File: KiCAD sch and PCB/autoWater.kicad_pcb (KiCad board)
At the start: 2 copper layers, 20.1 x 74.9 mm, 0 parts

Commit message: some commit
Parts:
- added C1: 0.1uF, Capacitor_SMD:C_0805_2012Metric_Pad1.15x1.40mm_HandSolder, F.Cu at (46.0, 79.0)
- added D1: LED, LED_SMD:LED_0805_2012Metric_Pad1.15x1.40mm_HandSolder, F.Cu at (53.0, 46.0)
- added J1: Li-ion 18650, Connector_PinHeader_2.54mm:PinHeader_1x02_P2.54mm_Vertical, F.Cu at (49.8, 79.0)
- added J2: PROG, Connector_PinHeader_2.54mm:PinHeader_1x05_P2.54mm_Vertical, F.Cu at (42.2, 67.8)
- added J3: Water Pump, Connector_PinHeader_2.54mm:PinHeader_1x02_P2.54mm_Vertical, F.Cu at (49.0, 62.0)
- added J4: Soil Humidity Sensor, Connector_PinHeader_2.54mm:PinHeader_1x02_P2.54mm_Vertical, F.Cu at (41.0, 60.0)
- added Q1: AO3400, Package_TO_SOT_SMD:SOT-23, F.Cu at (40.6, 53.3)
- added Q2: AO3400, Package_TO_SOT_SMD:SOT-23, F.Cu at (29.2, 54.1)
- added R1: 470, Resistor_SMD:R_0805_2012Metric_Pad1.15x1.40mm_HandSolder, F.Cu at (57.0, 62.0)
- added R2: 4.7k, Resistor_THT:R_Axial_DIN0411_L9.9mm_D3.6mm_P15.24mm_Horizontal, F.Cu at (30.2, 82.0)
- added R3: 1.5k, Resistor_THT:R_Axial_DIN0411_L9.9mm_D3.6mm_P15.24mm_Horizontal, F.Cu at (59.7, 73.2)
- added R4: 10k, Resistor_SMD:R_0805_2012Metric_Pad1.15x1.40mm_HandSolder, F.Cu at (39.4, 71.9)
- added R5: 10k, Resistor_SMD:R_0805_2012Metric_Pad1.15x1.40mm_HandSolder, F.Cu at (54.7, 77.3)
- added R6: 470k, Resistor_SMD:R_0805_2012Metric_Pad1.15x1.40mm_HandSolder, F.Cu at (49.0, 46.0)
- added R7: 150k, Resistor_SMD:R_0805_2012Metric_Pad1.15x1.40mm_HandSolder, F.Cu at (47.5, 67.3)
- added SW1: SW_Push_Dual, Button_Switch_SMD:SW_SPST_Omron_B3FS-100xP, F.Cu at (63.8, 86.2)
- added U1: ATtiny13-20SSU, Package_SO:SOIC-8_3.9x4.9mm_P1.27mm, F.Cu at (48.6, 73.5)
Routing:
- net Net-(J2-Pad1): track 0.00 -> 13.9 mm
- net Net-(J2-Pad3): track 0.00 -> 6.73 mm
- net +5V: track 0.00 -> 6.48 mm
- net Net-(J2-Pad2): track 0.00 -> 4.47 mm

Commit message: new pcb
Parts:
- C1, D1, J1, J2, J3, J4, Q1, Q2, R1, R2, R3, R4, R5, R6, R7, SW1, U1: moved to B.Cu
- moved D1 47.2 mm to (42.3, 91.9), turned to 180 degrees
- moved R6 44.2 mm to (42.3, 89.7), turned to 180 degrees
- moved Q1 36.8 mm to (46.1, 89.7), turned to 180 degrees
- moved J4 36.5 mm to (47.0, 96.0), turned to 0 degrees
- moved Q2 26.5 mm to (49.5, 71.3)
- moved R2 25.7 mm to (51.8, 96.0)
- moved R1 25.1 mm to (40.1, 80.5)
- moved SW1 24.3 mm to (54.0, 63.9)
- moved J2 14.2 mm to (42.9, 82.0)
- moved R7 13.8 mm to (46.0, 81.0), turned to 270 degrees
- moved J1 13.8 mm to (46.7, 65.5), turned to 90 degrees
- moved C1 7.88 mm to (45.7, 71.1), turned to 90 degrees
- moved R3 5.21 mm to (56.1, 77.0), turned to 270 degrees
- moved R4 4.13 mm to (40.1, 75.9)
- moved R5 3.88 mm to (55.1, 73.4), turned to 0 degrees
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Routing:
- net +5V: track 6.48 -> 44.9 mm
- net Net-(J2-Pad3): track 6.73 -> 25.4 mm, vias 0 -> 2
- net Net-(J3-Pad2): track 0.00 -> 15.3 mm
- net GND: track 0.00 -> 13.2 mm, vias 0 -> 4
- net Button: track 0.00 -> 11.3 mm
- net Net-(R2-Pad2): track 0.00 -> 11.0 mm
- net Net-(D1-Pad2): track 0.00 -> 10.9 mm
- net Net-(Q2-Pad1): track 0.00 -> 8.95 mm
- net Net-(J2-Pad1): track 13.9 -> 19.0 mm
- net Sensor: track 0.00 -> 4.83 mm
- net Sensor_Voltage: track 0.00 -> 2.85 mm
- net Net-(J2-Pad2): track 4.47 -> 6.50 mm
- added copper zone on B.Cu, net GND
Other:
- board size 20.1 x 74.9 mm -> 20.8 x 41.4 mm

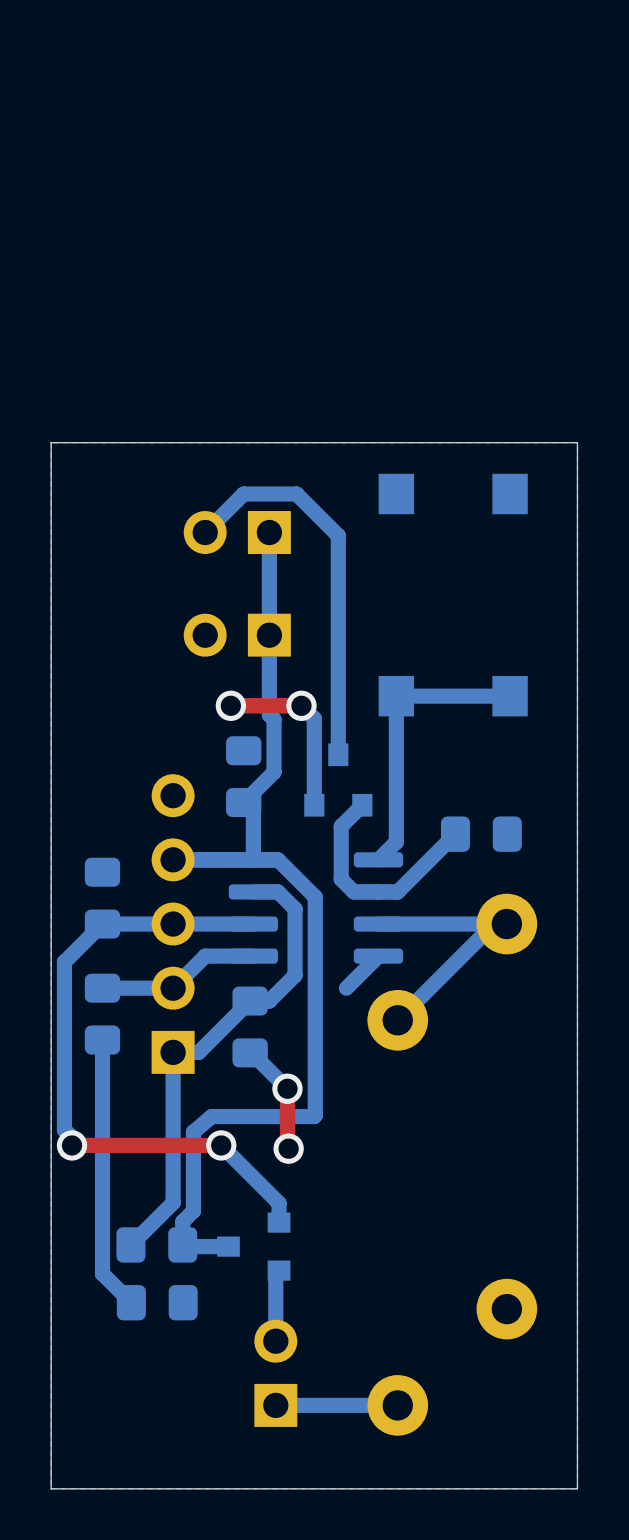
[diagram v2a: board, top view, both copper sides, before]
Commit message: added li ion charger on pcb
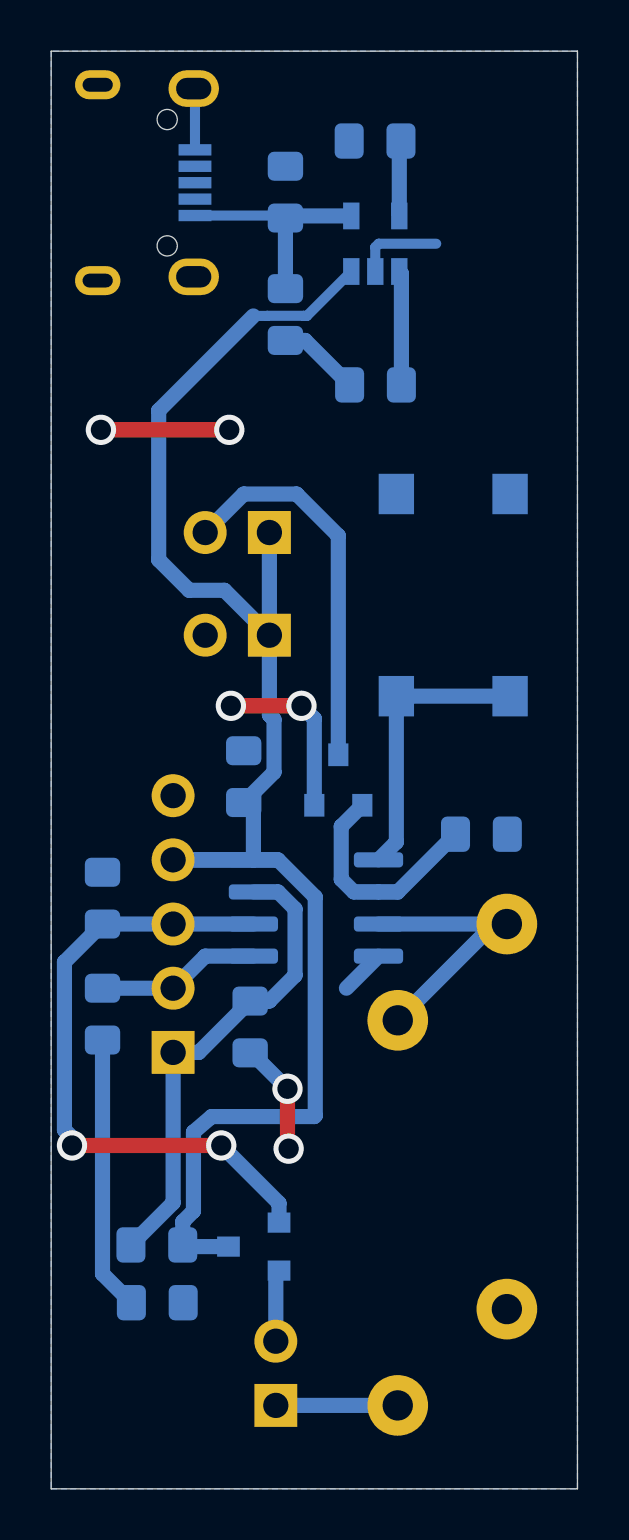
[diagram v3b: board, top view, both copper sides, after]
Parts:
- added C2: 4.7u, Capacitor_SMD:C_0805_2012Metric_Pad1.15x1.40mm_HandSolder, B.Cu at (47.4, 48.0)
- added D2: LED, LED_SMD:LED_0805_2012Metric_Pad1.15x1.40mm_HandSolder, B.Cu at (47.4, 52.8)
- added J5: USB_B_Micro, Connector_USB:USB_Micro-B_Wuerth_629105150521, B.Cu at (41.9, 47.6)
- added R8: 2k, Resistor_SMD:R_0805_2012Metric_Pad1.15x1.40mm_HandSolder, B.Cu at (50.9, 46.0)
- added R9: 470, Resistor_SMD:R_0805_2012Metric_Pad1.15x1.40mm_HandSolder, B.Cu at (50.9, 55.6)
- added U2: MCP73831-2-OT, Package_TO_SOT_SMD:SOT-23-5, B.Cu at (50.9, 50.0)
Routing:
- net +5V: track 44.9 -> 66.3 mm
- net GND: track 13.2 -> 24.2 mm, vias 4 -> 6
- net Net-(C2-Pad1): track 0.00 -> 9.06 mm
- net Net-(R9-Pad2): track 0.00 -> 4.52 mm
- net Net-(D2-Pad1): track 0.00 -> 3.27 mm
- net Net-(R8-Pad1): track 0.00 -> 2.99 mm
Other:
- board size 20.8 x 41.4 mm -> 20.8 x 56.9 mm

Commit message: resistor value change
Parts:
- R2: value 4.7k -> 6.8k
- R6: value 470k -> 680k
